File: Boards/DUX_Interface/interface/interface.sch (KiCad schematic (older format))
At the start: 14 parts, among them J1 MM_F_VT_20, J2 MM_F_VT_20, J3 MM_F_VT_04, J4 MM_F_VT_10, J5 MM_F_VT_04, J7 Ampseal_35_VT, J8 MicroFit_RA_V_2, U1 Nanofit_12, U2 Nanofit_4, U3 Nanofit_4, U4 Nanofit_10, U5 RJ45_VT, U6 RJ45_VT

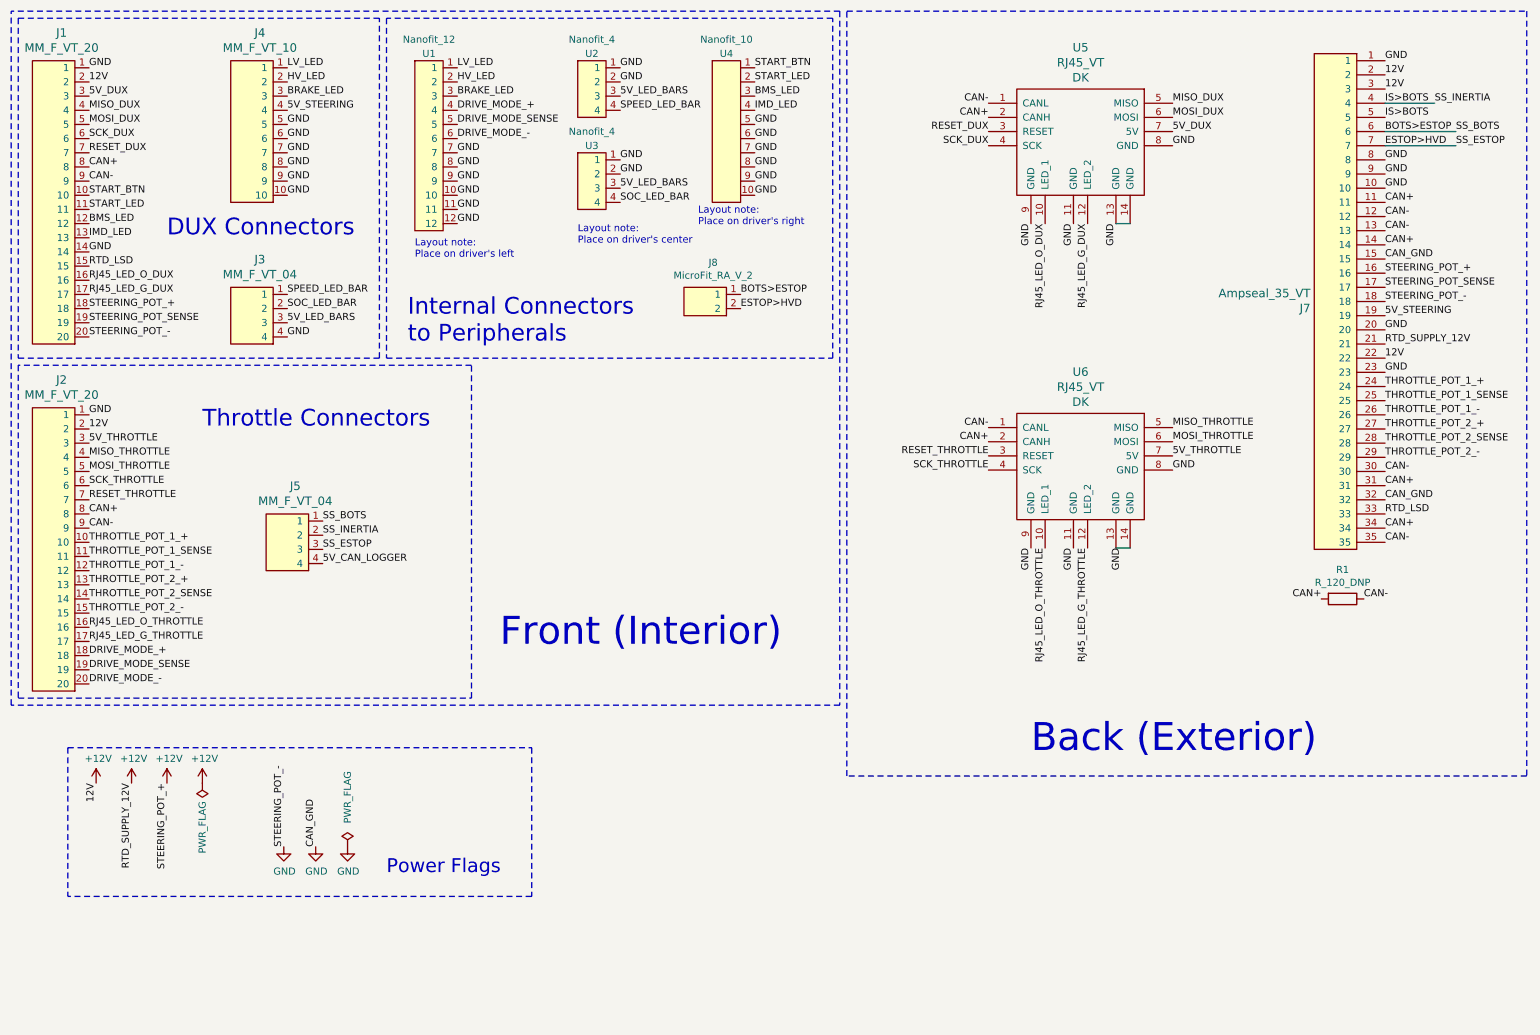
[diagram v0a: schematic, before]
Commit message: test points and silkscreen
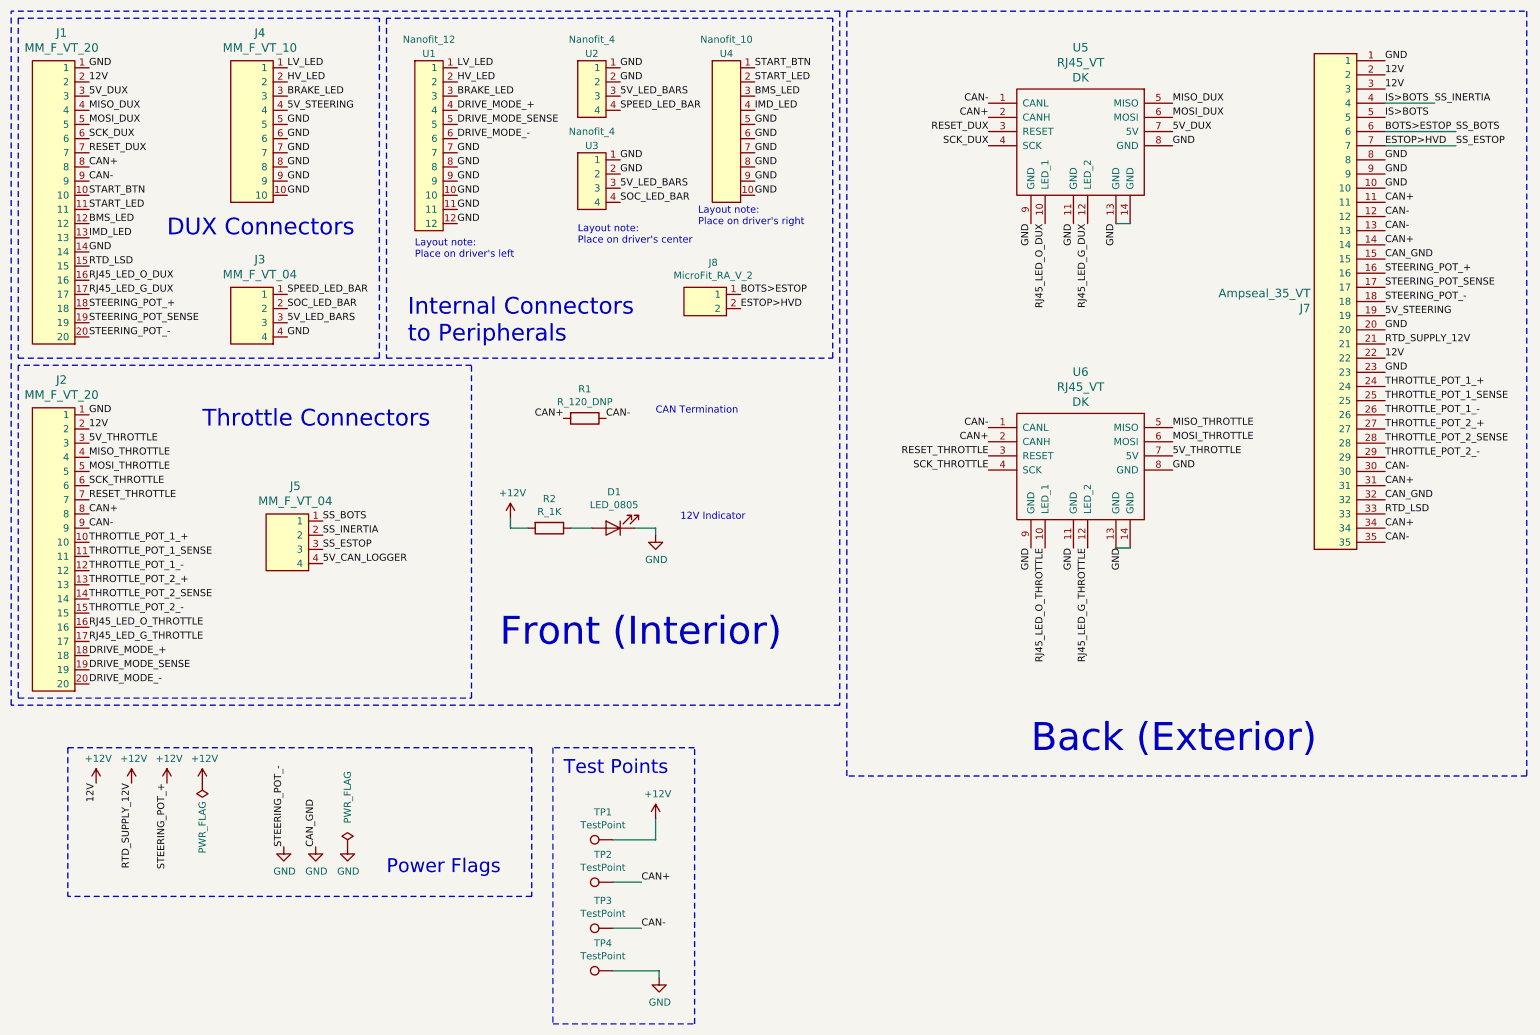
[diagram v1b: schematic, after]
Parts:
- added D1: LED_0805, footprints:LED_0805_OEM, symbol formula:LED_0805
- added R2: R_1K, footprints:R_0805_OEM, symbol formula:R_1K
- added TP1, TP2, TP3, TP4: TestPoint, footprints:tp_1.6mm, symbol Connector:TestPoint
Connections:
- net +12V: now also R2.2, TP1.1
- net CAN+: now also TP2.1
- net CAN-: now also TP3.1
- net GND: now also D1.1 (K), TP4.1
- new net: D1.2 (A), R2.1
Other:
- note added: "12V Indicator"
- note added: "CAN Termination"
- note added: "Test Points"
- moved on the sheet: R1
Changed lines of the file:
@@
 L formula:R_120_DNP R1
 U 1 1 5DD2F1A4
-P 9900 4650
-F 0 "R1" V 9693 4650 50  0000 C CNN
-F 1 "R_120_DNP" V 9784 4650 50  0000 C CNN
-F 2 "footprints:R_0805_OEM" H 8700 4800 50  0001 L CNN
-F 3 "https://www.mouser.com/datasheet/2/315/AOA0000C304-1149620.pdf" H 8700 5100 50  0001 L CNN
-F 4 "DK" H 9900 4650 60  0001 C CNN "MFN"
-F 5 "667-ERJ-6ENF1200V" H 8700 4900 60  0001 L CNN "MPN"
-F 6 "https://www.mouser.com/ProductDetail/Panasonic-Industrial-Devices/ERJ-6ENF1200V?qs=sGAEpiMZZMvdGkrng054t8AJgcdMkx7x%252bFQnctTMUmU%3d" H 8700 5000 60  0001 L CNN "PurchasingLink"
-	1    9900 4650
+P 4550 3375
+F 0 "R1" V 4343 3375 50  0000 C CNN
+F 1 "R_120_DNP" V 4434 3375 50  0000 C CNN
+F 2 "footprints:R_0805_OEM" H 3350 3525 50  0001 L CNN
+F 3 "https://www.mouser.com/datasheet/2/315/AOA0000C304-1149620.pdf" H 3350 3825 50  0001 L CNN
+F 4 "DK" H 4550 3375 60  0001 C CNN "MFN"
+F 5 "667-ERJ-6ENF1200V" H 3350 3625 60  0001 L CNN "MPN"
+F 6 "https://www.mouser.com/ProductDetail/Panasonic-Industrial-Devices/ERJ-6ENF1200V?qs=sGAEpiMZZMvdGkrng054t8AJgcdMkx7x%252bFQnctTMUmU%3d" H 3350 3725 60  0001 L CNN "PurchasingLink"
+	1    4550 3375
 	0    1    1    0
 $EndComp
-Text Label 9750 4650 2    50   ~ 0
+Text Label 4400 3375 2    50   ~ 0
 CAN+
-Text Label 10050 4650 0    50   ~ 0
+Text Label 4700 3375 0    50   ~ 0
 CAN-
 $Comp
@@
 STEERING_POT_-
 $Comp
-L power:+12V #PWR?
+L power:+12V #PWR0101
 U 1 1 5E63233C
 P 1600 5950
-F 0 "#PWR?" H 1600 5800 50  0001 C CNN
+F 0 "#PWR0101" H 1600 5800 50  0001 C CNN
 F 1 "+12V" H 1615 6123 50  0000 C CNN
 F 2 "" H 1600 5950 50  0001 C CNN
@@
 $EndComp
 $Comp
-L power:GND #PWR?
+L power:GND #PWR0102
 U 1 1 5E63537E
 P 2425 6400
-F 0 "#PWR?" H 2425 6150 50  0001 C CNN
+F 0 "#PWR0102" H 2425 6150 50  0001 C CNN
 F 1 "GND" H 2430 6227 50  0000 C CNN
 F 2 "" H 2425 6400 50  0001 C CNN
@@
 Wire Notes Line
 	900  5700 900  6750
+$Comp
+L Connector:TestPoint TP1
+U 1 1 5E65DC3E
+P 4750 6350
+F 0 "TP1" V 4945 6422 50  0000 C CNN
+F 1 "TestPoint" V 4854 6422 50  0000 C CNN
+F 2 "footprints:tp_1.6mm" H 4950 6350 50  0001 C CNN
+F 3 "~" H 4950 6350 50  0001 C CNN
+	1    4750 6350
+	0    -1   -1   0
+$EndComp
+$Comp
+L Connector:TestPoint TP2
+U 1 1 5E65EA13
+P 4750 6650
+F 0 "TP2" V 4945 6722 50  0000 C CNN
+F 1 "TestPoint" V 4854 6722 50  0000 C CNN
+F 2 "footprints:tp_1.6mm" H 4950 6650 50  0001 C CNN
+F 3 "~" H 4950 6650 50  0001 C CNN
+	1    4750 6650
+	0    -1   -1   0
+$EndComp
+$Comp
+L Connector:TestPoint TP3
+U 1 1 5E65F584
+P 4750 6975
+F 0 "TP3" V 4945 7047 50  0000 C CNN
+F 1 "TestPoint" V 4854 7047 50  0000 C CNN
+F 2 "footprints:tp_1.6mm" H 4950 6975 50  0001 C CNN
+F 3 "~" H 4950 6975 50  0001 C CNN
+	1    4750 6975
+	0    -1   -1   0
+$EndComp
+$Comp
+L Connector:TestPoint TP4
+U 1 1 5E65F58A
+P 4750 7275
+F 0 "TP4" V 4945 7347 50  0000 C CNN
+F 1 "TestPoint" V 4854 7347 50  0000 C CNN
+F 2 "footprints:tp_1.6mm" H 4950 7275 50  0001 C CNN
+F 3 "~" H 4950 7275 50  0001 C CNN
+	1    4750 7275
+	0    -1   -1   0
+$EndComp
+Text Label 4950 6650 0    50   ~ 0
+CAN+
+Text Label 4950 6975 0    50   ~ 0
+CAN-
+Wire Wire Line
+	4950 6975 4750 6975
+$Comp
+L power:GND #PWR09
+U 1 1 5E6612D4
+P 5075 7325
+F 0 "#PWR09" H 5075 7075 50  0001 C CNN
+F 1 "GND" H 5080 7152 50  0000 C CNN
+F 2 "" H 5075 7325 50  0001 C CNN
+F 3 "" H 5075 7325 50  0001 C CNN
+	1    5075 7325
+	1    0    0    -1
+$EndComp
+Wire Wire Line
+	5075 7325 5075 7275
+Wire Wire Line
+	5075 7275 4750 7275
+$Comp
+L power:+12V #PWR08
+U 1 1 5E6644FB
+P 5050 6200
+F 0 "#PWR08" H 5050 6050 50  0001 C CNN
+F 1 "+12V" H 5065 6373 50  0000 C CNN
+F 2 "" H 5050 6200 50  0001 C CNN
+F 3 "" H 5050 6200 50  0001 C CNN
+	1    5050 6200
+	1    0    0    -1
+$EndComp
+Wire Wire Line
+	5050 6200 5050 6350
+Wire Wire Line
+	5050 6350 4750 6350
+Wire Wire Line
+	4750 6650 4950 6650
+Text Notes 4400 5900 0    98   ~ 0
+Test Points
+Wire Notes Line
+	4325 5700 4325 7650
+Wire Notes Line
+	4325 7650 5325 7650
+Wire Notes Line
+	5325 7650 5325 5700
+Wire Notes Line
+	5325 5700 4325 5700
+$Comp
+L formula:R_1K R2
+U 1 1 5E67032C
+P 4300 4150
+F 0 "R2" V 4093 4150 50  0000 C CNN
+F 1 "R_1K" V 4184 4150 50  0000 C CNN
+F 2 "footprints:R_0805_OEM" H 4230 4150 50  0001 C CNN
+F 3 "https://www.seielect.com/Catalog/SEI-rncp.pdf" H 4380 4150 50  0001 C CNN
+F 4 "DK" H 4300 4150 60  0001 C CNN "MFN"
+F 5 "RNCP0805FTD1K00CT-ND" H 4300 4150 60  0001 C CNN "MPN"
+F 6 "https://www.digikey.com/products/en?keywords=RNCP0805FTD1K00CT-ND" H 4780 4550 60  0001 C CNN "PurchasingLink"
+	1    4300 4150
+	0    1    1    0
+$EndComp
+$Comp
+L formula:LED_0805 D1
+U 1 1 5E671943
+P 4750 4150
+F 0 "D1" H 4743 3895 50  0000 C CNN
+F 1 "LED_0805" H 4743 3986 50  0000 C CNN
+F 2 "footprints:LED_0805_OEM" H 4650 4150 50  0001 C CNN
+F 3 "http://www.osram-os.com/Graphics/XPic9/00078860_0.pdf" H 4750 4250 50  0001 C CNN
+F 4 "DK" H 4750 4150 60  0001 C CNN "MFN"
+F 5 "475-1410-1-ND" H 4750 4150 60  0001 C CNN "MPN"
+F 6 "https://www.digikey.com/products/en?keywords=475-1410-1-ND" H 5150 4650 60  0001 C CNN "PurchasingLink"
+	1    4750 4150
+	-1   0    0    1
+$EndComp
+Wire Wire Line
+	4450 4150 4600 4150
+$Comp
+L power:+12V #PWR06
+U 1 1 5E675CE9
+P 4025 4075
+F 0 "#PWR06" H 4025 3925 50  0001 C CNN
+F 1 "+12V" H 4040 4248 50  0000 C CNN
+F 2 "" H 4025 4075 50  0001 C CNN
+F 3 "" H 4025 4075 50  0001 C CNN
+	1    4025 4075
+	1    0    0    -1
+$EndComp
+Wire Wire Line
+	4025 4075 4025 4150
+Wire Wire Line
+	4025 4150 4150 4150
+$Comp
+L power:GND #PWR07
+U 1 1 5E678C29
+P 5050 4200
+F 0 "#PWR07" H 5050 3950 50  0001 C CNN
+F 1 "GND" H 5055 4027 50  0000 C CNN
+F 2 "" H 5050 4200 50  0001 C CNN
+F 3 "" H 5050 4200 50  0001 C CNN
+	1    5050 4200
+	1    0    0    -1
+$EndComp
+Wire Wire Line
+	5050 4200 5050 4150
+Wire Wire Line
+	4900 4150 5050 4150
+Text Notes 5050 3350 0    50   ~ 0
+CAN Termination
+Text Notes 5225 4100 0    50   ~ 0
+12V Indicator
 $EndSCHEMATC
